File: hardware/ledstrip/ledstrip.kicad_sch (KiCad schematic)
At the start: 14 parts, among them J1 Conn_ARM_JTAG_SWD_10, J2 USB_C_Receptacle_USB2.0_16P, U1 STM32G030K6Tx, U2 CP2102N-A02-GQFN20, U4 USBLC6-2SC6

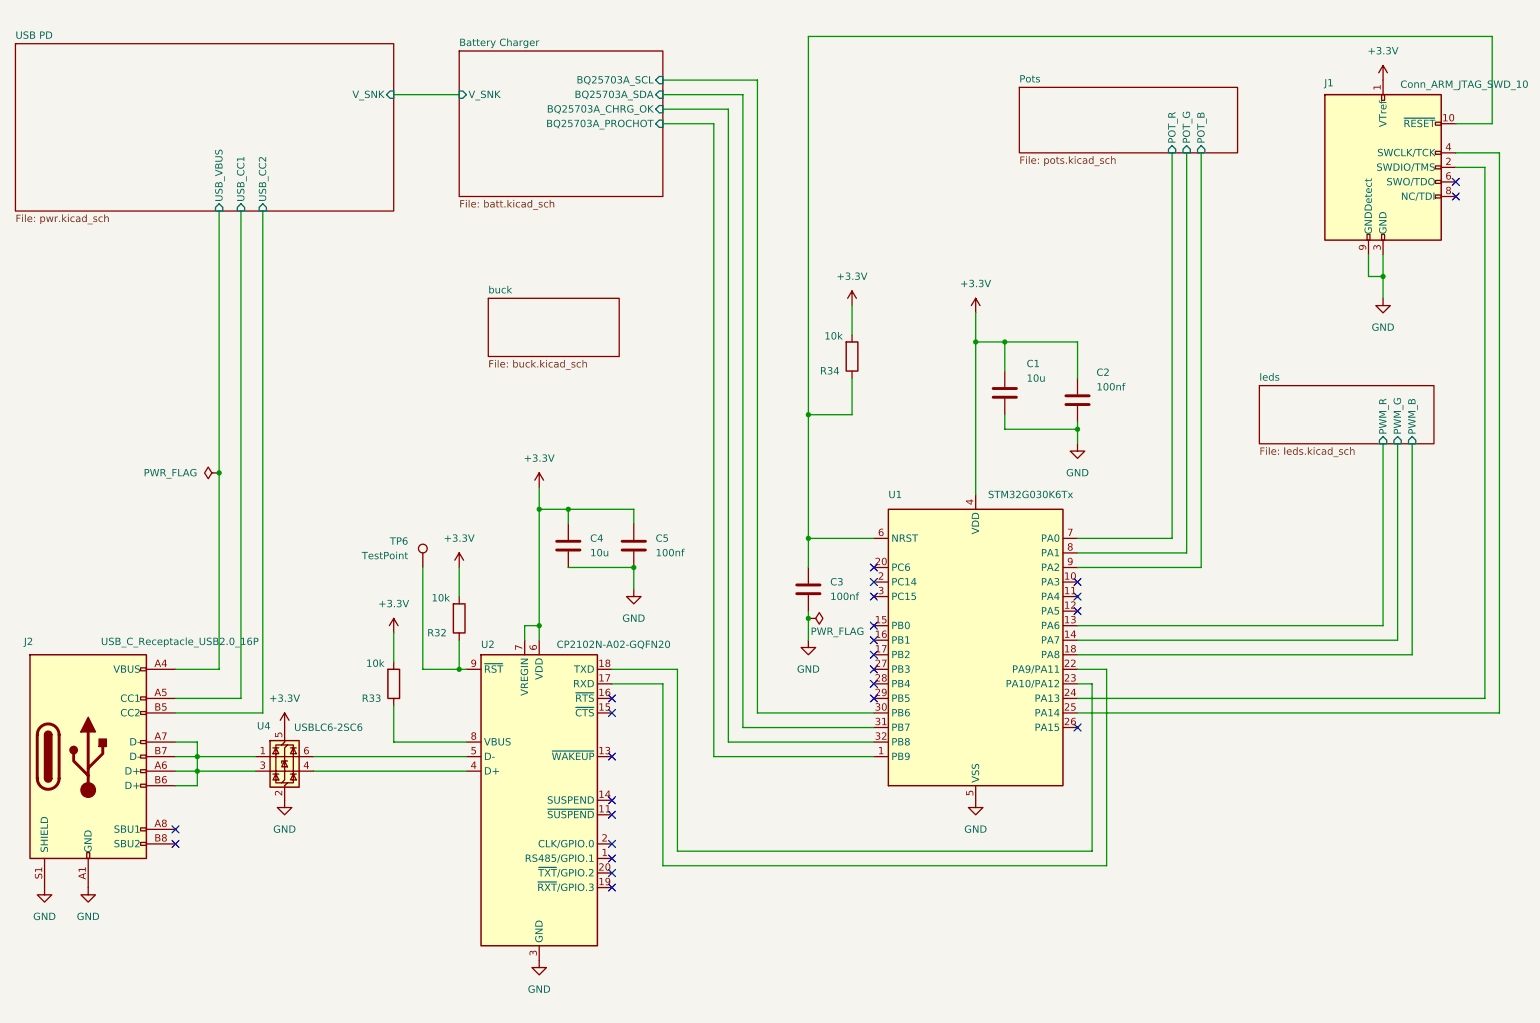
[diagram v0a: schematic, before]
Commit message: Add label on nodes.
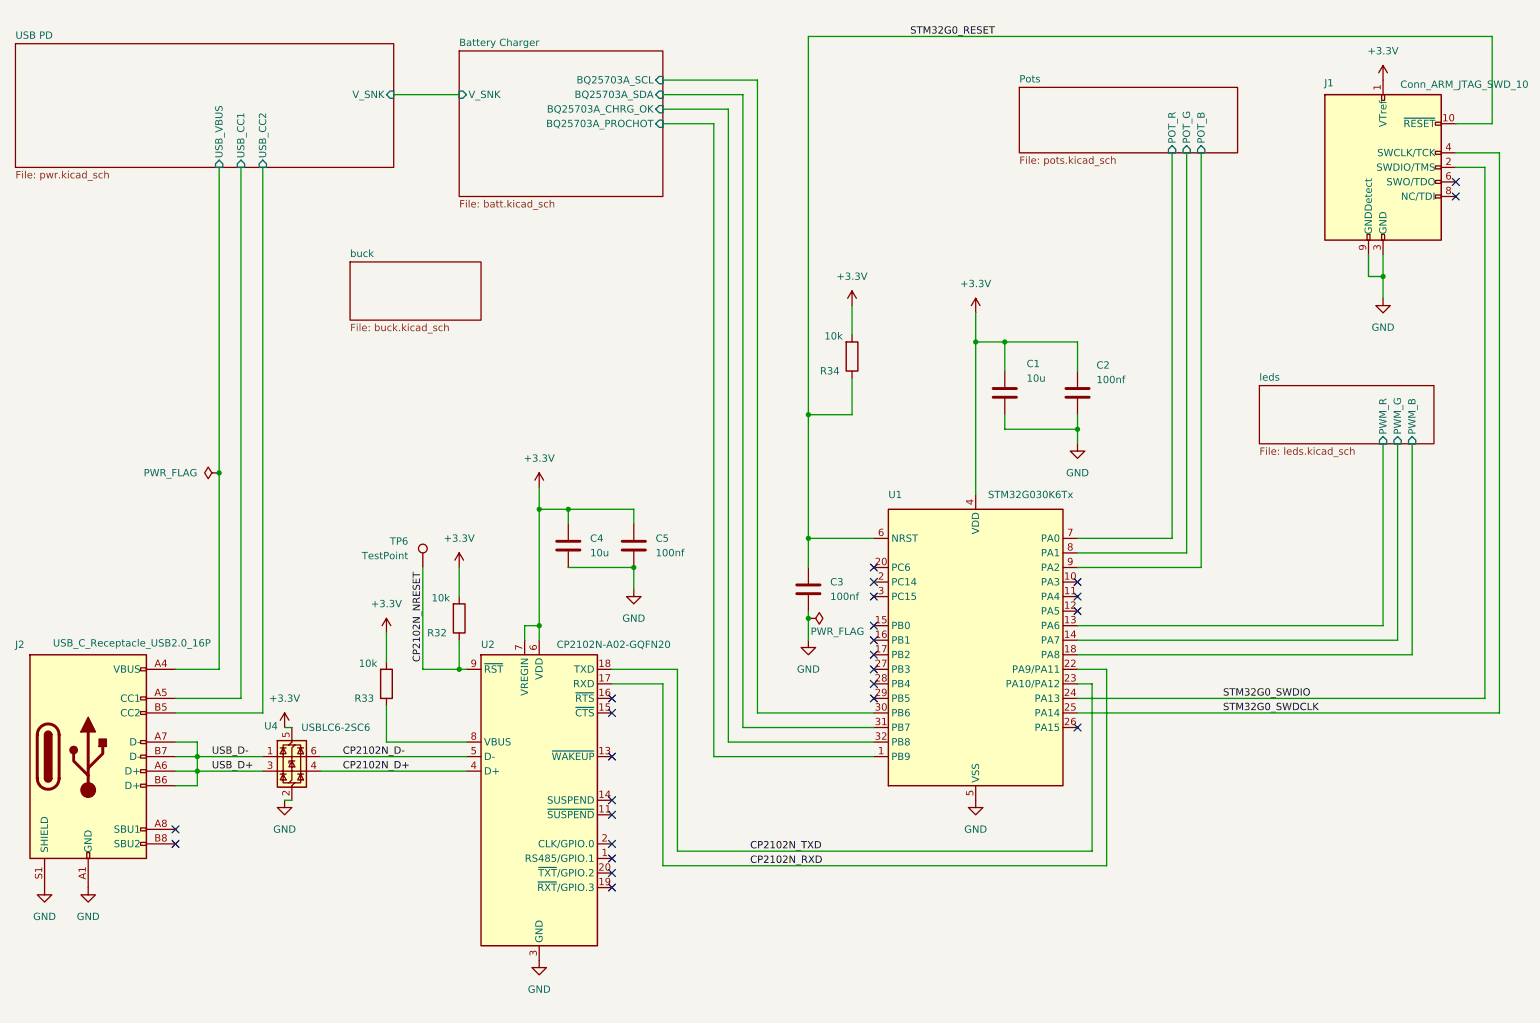
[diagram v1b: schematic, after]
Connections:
- net USB_D+: now reaches J2.A6 (D+), J2.A7 (D-), J2.B6 (D+), J2.B7 (D-), U4.1 (I/O1), U4.3 (I/O2)
- net CP2102N_RXD: now reaches U1.22 (PA9/PA11), U2.17 (RXD)
- net CP2102N_TXD: now reaches U1.23 (PA10/PA12), U2.18 (TXD)
- net CP2102N_D+: now reaches U2.4 (D+), U4.4 (I/O2)
- net CP2102N_D-: now reaches U2.5 (D-), U4.6 (I/O1)
- net CP2102N_NRESET: now reaches R32.1, TP6.1, U2.9 (~{RST})
- net STM32G0_RESET: now reaches C3.1, J1.10 (~{RESET}), R34.1, U1.6 (NRST)
- net STM32G0_SWDIO: now reaches J1.2 (SWDIO/TMS), U1.24 (PA13)
- net STM32G0_SWDCLK: now reaches J1.4 (SWCLK/TCK), U1.25 (PA14)
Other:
- moved on the sheet: C2, R33, U4

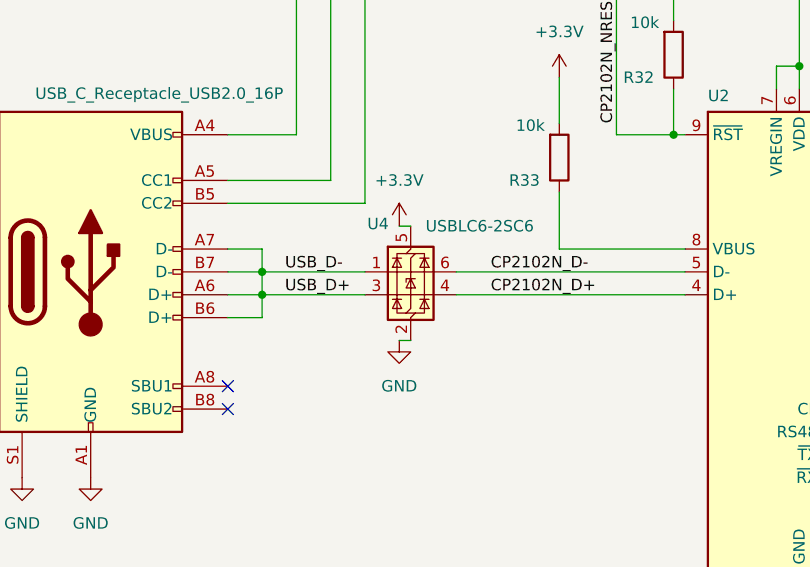
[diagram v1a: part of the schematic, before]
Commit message: Added a pull down to VSYS
(external powered if header connected, otherwise VSYS is tied to GND) in STUSB4500 integration.
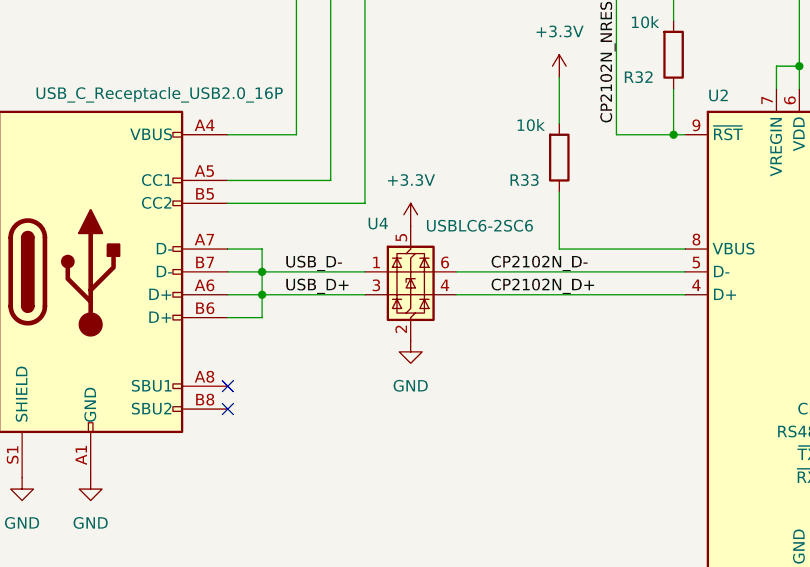
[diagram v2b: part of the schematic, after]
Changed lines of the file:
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@@
-	(wire
-		(pts
-			(xy 67.31 151.13) (xy 66.04 151.13)
-		)
-		(stroke
-			(width 0)
-			(type default)
-		)
-	)
 	(wire
 		(pts
@@
 		(pts
 			(xy 257.81 120.65) (xy 257.81 88.9)
-		)
-		(stroke
-			(width 0)
-			(type default)
-		)
-	)
-	(wire
-		(pts
-			(xy 67.31 138.43) (xy 66.04 138.43)
 		)
 		(stroke
@@
 	(symbol
 		(lib_id "power:GND")
-		(at 66.04 151.13 0)
+		(at 67.31 151.13 0)
 		(unit 1)
 		(exclude_from_sim no)
@@
 		(fields_autoplaced yes)
 		(property "Reference" "#PWR09"
-			(at 66.04 157.48 0)
+			(at 67.31 157.48 0)
 			(effects
 				(font
@@
 		)
 		(property "Value" "GND"
-			(at 66.04 156.21 0)
+			(at 67.31 156.21 0)
 			(effects
 				(font
@@
 		)
 		(property "Footprint" ""
-			(at 66.04 151.13 0)
+			(at 67.31 151.13 0)
 			(effects
 				(font
@@
 		)
 		(property "Datasheet" ""
-			(at 66.04 151.13 0)
+			(at 67.31 151.13 0)
 			(effects
 				(font
@@
 		)
 		(property "Description" "Power symbol creates a global label with name \"GND\" , ground"
-			(at 66.04 151.13 0)
+			(at 67.31 151.13 0)
 			(effects
 				(font
@@
 	(symbol
 		(lib_id "power:+3.3V")
-		(at 66.04 138.43 0)
+		(at 67.31 138.43 0)
 		(unit 1)
 		(exclude_from_sim no)
@@
 		(fields_autoplaced yes)
 		(property "Reference" "#PWR019"
-			(at 66.04 142.24 0)
+			(at 67.31 142.24 0)
 			(effects
 				(font
@@
 		)
 		(property "Value" "+3.3V"
-			(at 66.04 133.35 0)
+			(at 67.31 133.35 0)
 			(effects
 				(font
@@
 		)
 		(property "Footprint" ""
-			(at 66.04 138.43 0)
+			(at 67.31 138.43 0)
 			(effects
 				(font
@@
 		)
 		(property "Datasheet" ""
-			(at 66.04 138.43 0)
+			(at 67.31 138.43 0)
 			(effects
 				(font
@@
 		)
 		(property "Description" "Power symbol creates a global label with name \"+3.3V\""
-			(at 66.04 138.43 0)
-			(effects
-				(font
+			(at 67.31 138.43 0)
+			(effects
+				(font

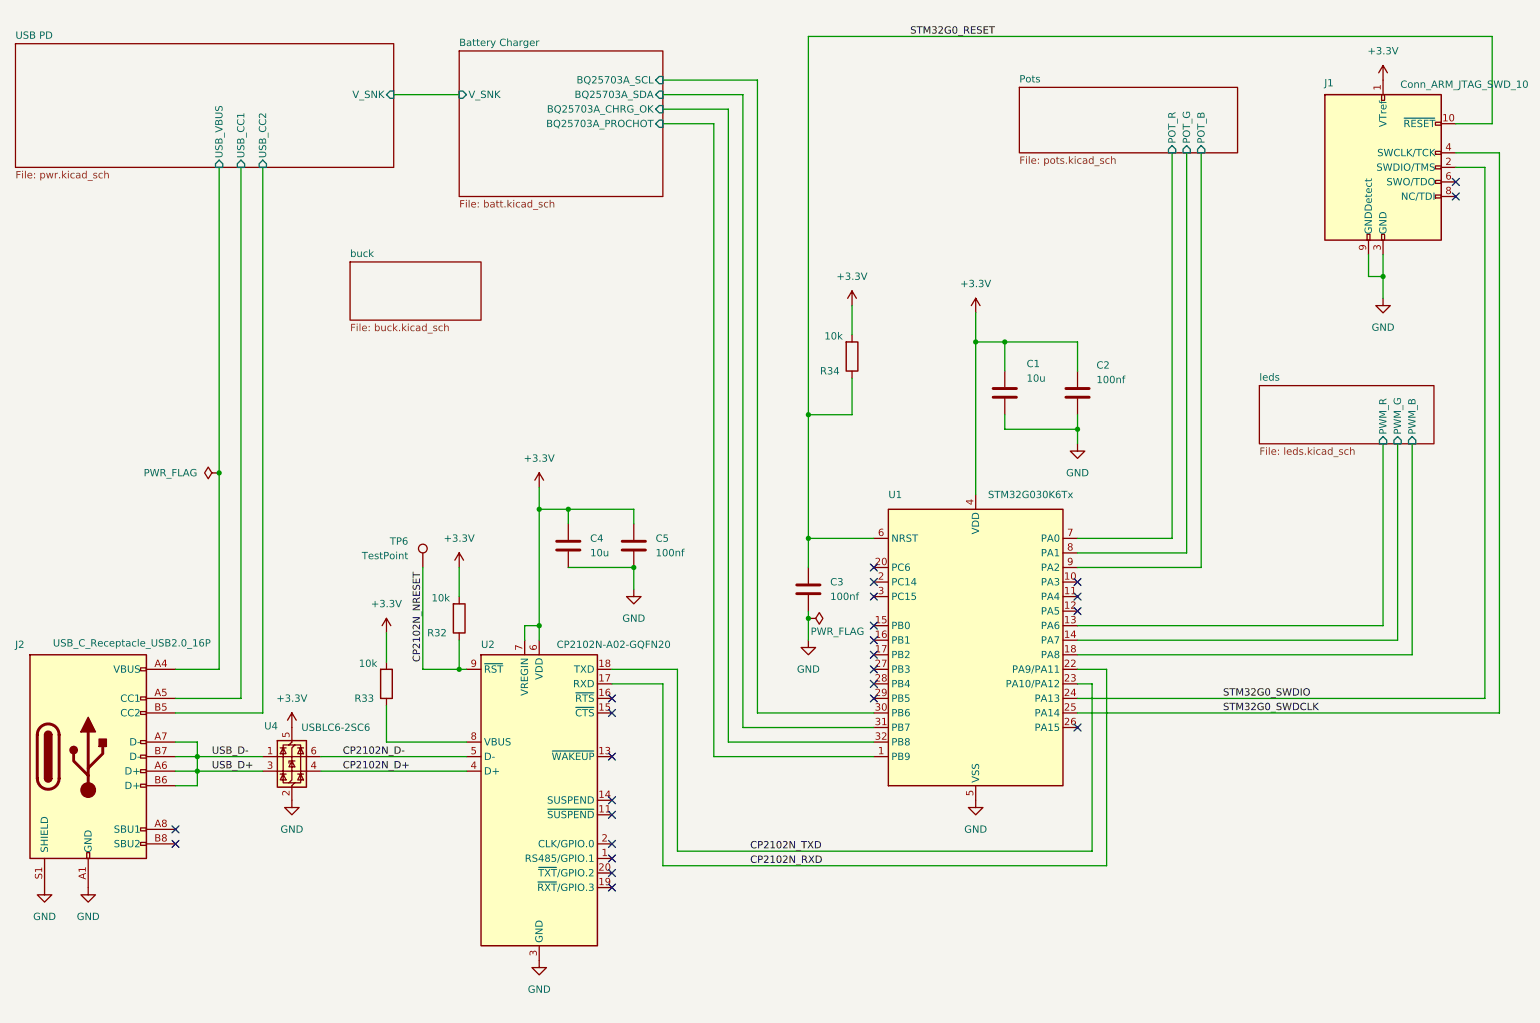
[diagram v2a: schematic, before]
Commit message: Continue PCB.
Create netlists and color them.
Fix wrong symbol pin <-> foot print pins mapping.
Replace footprint and part for leds N-MOSFET.
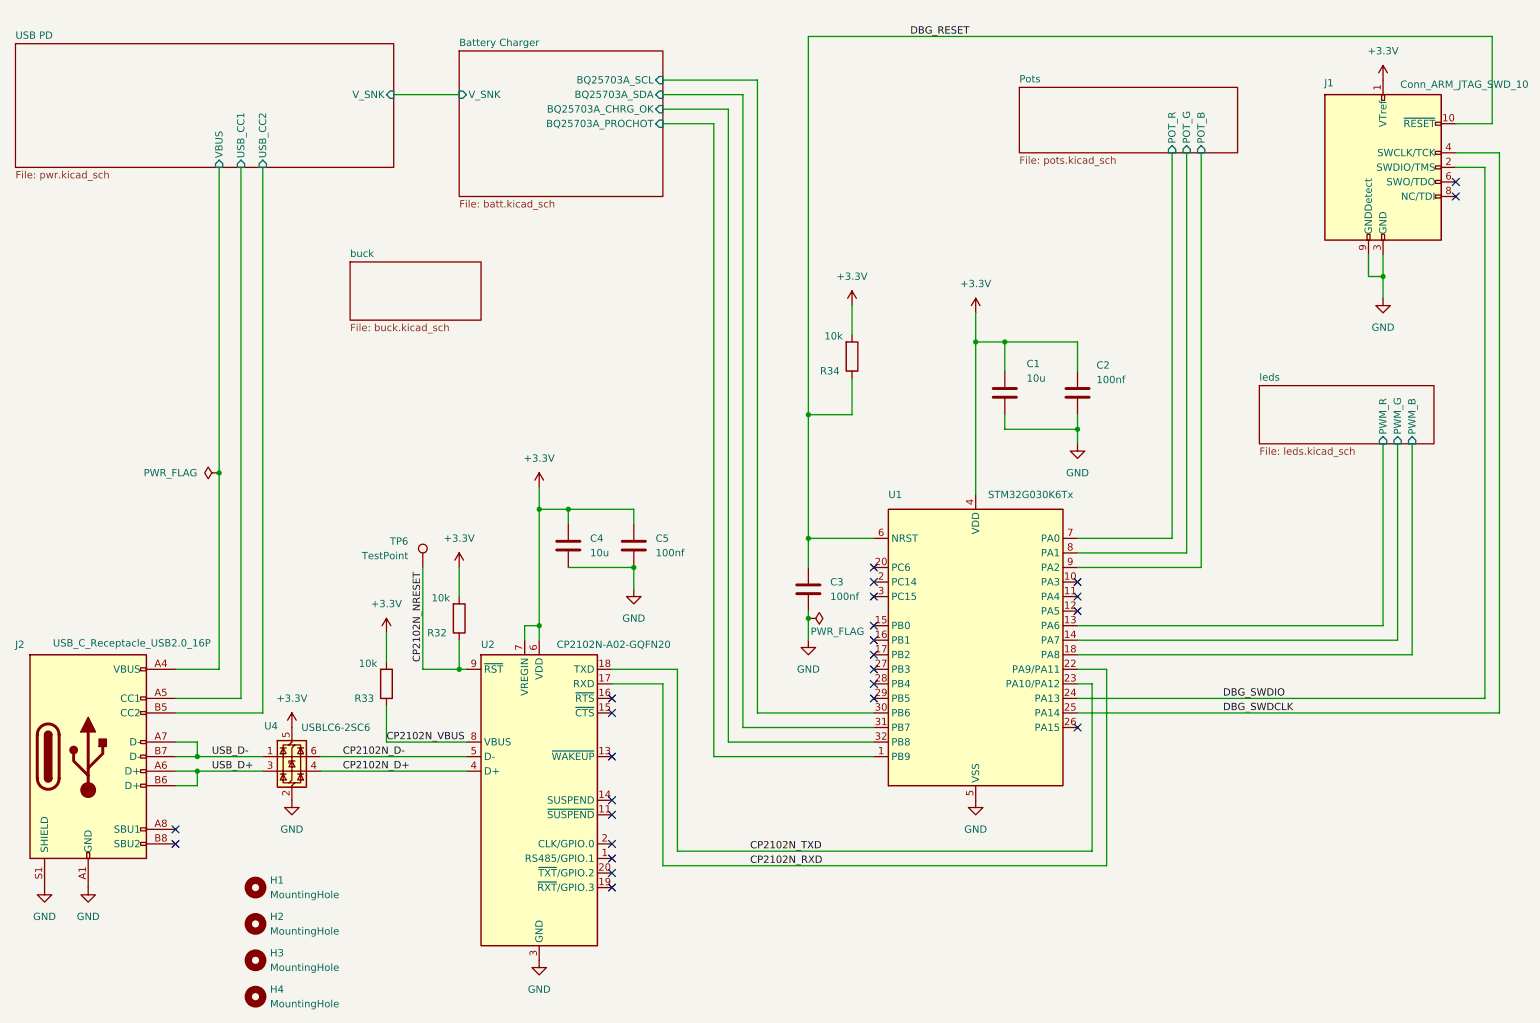
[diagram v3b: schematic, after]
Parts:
- added H1, H2, H3, H4: MountingHole, MountingHole:MountingHole_3.2mm_M3, symbol Mechanical:MountingHole
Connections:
- net USB_D+: no longer J2.A7 (D-), J2.B7 (D-), U4.1 (I/O1)
- net CP2102N_VBUS: now reaches R33.1, U2.8 (VBUS)
- net STM32G0_RESET renamed DBG_RESET
- net STM32G0_SWDCLK renamed DBG_SWDCLK
- net STM32G0_SWDIO renamed DBG_SWDIO
- net USB PD/USB_VBUS renamed USB PD/VBUS
- new net USB_D-: J2.A7 (D-), J2.B7 (D-), U4.1 (I/O1)
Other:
- sheet USB PD ports: added VBUS; removed USB_VBUS
